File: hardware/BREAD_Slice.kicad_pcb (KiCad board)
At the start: 2 copper layers, 70 x 100 mm, 59 parts, among them J1 Conn_01x10_Socket, J2 Screw_Terminal_01x06, J3 Screw_Terminal_01x02, J4 Screw_Terminal_01x08, SW1 SW_DIP_x04, SW3 SW_SPDT, U1 AP63205, U10 CPC1002N, U11 CPC1002N, U12 NTGS4111PT1G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

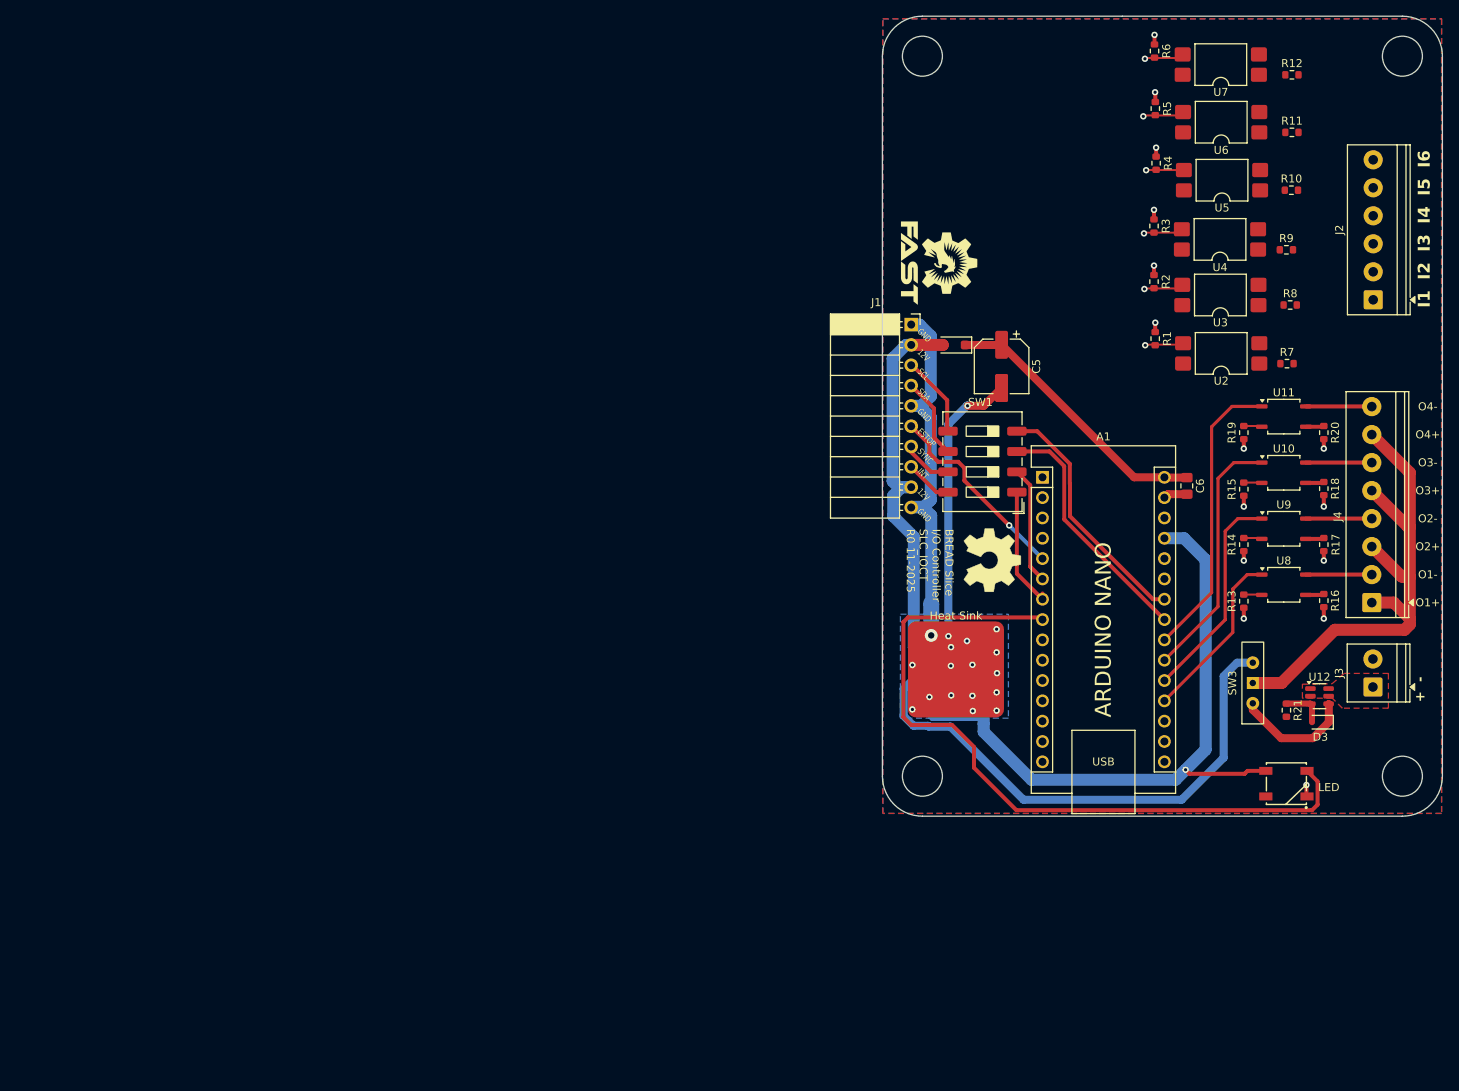
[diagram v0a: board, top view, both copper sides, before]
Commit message: revision of symbol attachment and clear out old layout and start new; kml-custom to kmlib-local
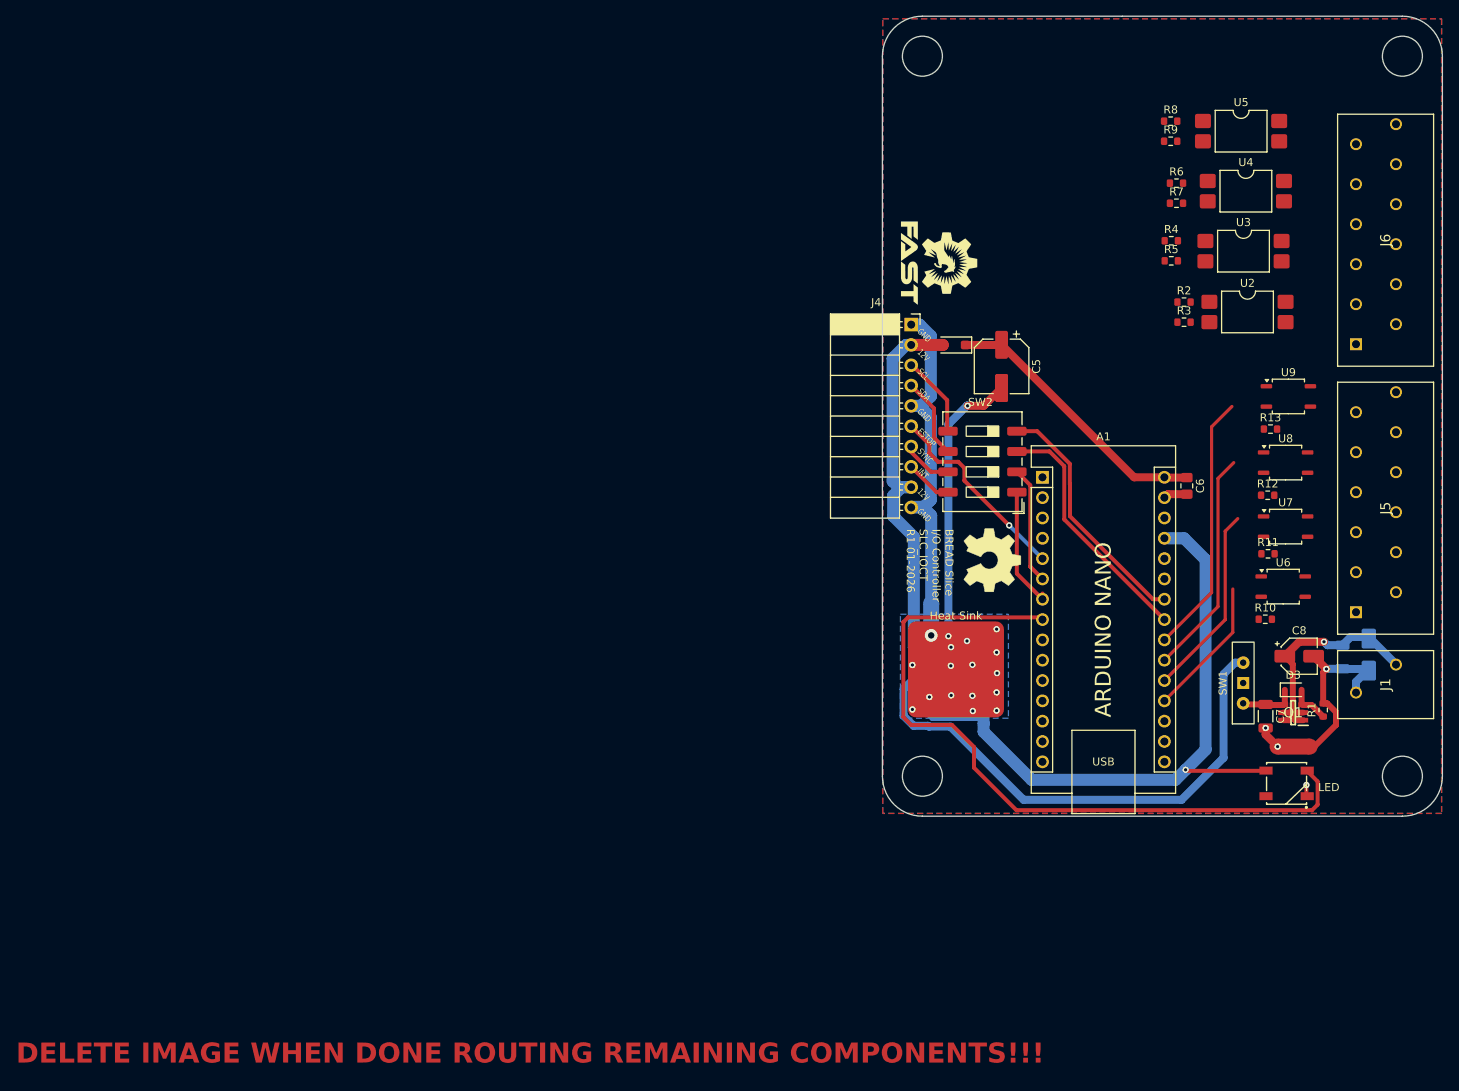
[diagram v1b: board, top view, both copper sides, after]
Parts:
- removed J2: Screw_Terminal_01x06, TerminalBlock_Phoenix:TerminalBlock_Phoenix_PT-1,5-6-3.5-H_1x06_P3.50mm_Horizontal
- removed J3: Screw_Terminal_01x02, TerminalBlock_Phoenix:TerminalBlock_Phoenix_PT-1,5-2-3.5-H_1x02_P3.50mm_Horizontal
- removed the J4 at (183.8, 113.1)
- removed R14, R15, R19: 2.4k, Resistor_SMD:R_0603_1608Metric
- removed R16, R17, R18, R20: 47, Resistor_SMD:R_0603_1608Metric
- removed R21: 100k, Resistor_SMD:R_0603_1608Metric
- removed U10, U11: CPC1002N, Package_SO:SOP-4_3.8x4.1mm_P2.54mm
- removed U12: NTGS4111PT1G, Package_TO_SOT_SMD:TSOT-23-6
- added C7: 100n, Capacitor_SMD:C_1206_3216Metric, F.Cu at (170.5, 127.3)
- added C8: 10u, Capacitor_SMD:CP_Elec_4x5.8, F.Cu at (174.7, 119.8)
- added C9: 100n, Capacitor_SMD:C_1206_3216Metric, B.Cu at (180.1, 119.9)
- added D4: SMAJ24CA, Diode_SMD:D_SMA, B.Cu at (183.4, 119.6)
- added J1: 1985195, KMLib_Connectors:1985195, F.Cu at (181.8, 127.6)
- added J5: 1990106, KMLib_Connectors:1990106, F.Cu at (181.8, 114.3)
- added J6: 1990106, KMLib_Connectors:1990106, F.Cu at (181.8, 80.8)
- added NT2: NetTie_2, NetTie:NetTie-2_SMD_Pad2.0mm, F.Cu at (174.0, 131.1)
- added Q1: NTGS4111PT1G, KMLib_IC_SMD:SOT95P275X110-6N, F.Cu at (173.9, 126.8)
- A1: footprint kml-custom:Arduino_Nano_Headers -> KMLib_Boards_Modules:Arduino_Nano_Headers
- D2: footprint kml-custom:WS2812-5050-4PIN -> KMLib_IC_SMD:WS2812-5050-4PIN
- HS1: footprint kml-custom:Thermal Pad -> KMLib_Mounting:Thermal Pad
- R1: value 1k -> 100k
- R10, R11, R12: value 1k -> 1.3k
- R13: value 2.4k -> 1.3k
- U1: footprint kml-custom:SOIC_05WU-7_DIO-M -> KMLib_IC_SMD:SOIC_05WU-7_DIO
- U6, U7: value LTV-817S -> CPC1002N; footprint Package_DIP:SMDIP-4_W9.53mm -> Package_SO:SOP-4_3.8x4.1mm_P2.54mm
- moved U6 58.6 mm to (172.7, 111.1), turned to 0 degrees
- moved U7 58.3 mm to (173.0, 103.6), turned to 0 degrees
- moved R10 53.7 mm to (170.5, 115.2)
- moved R11 52.8 mm to (170.8, 107.0)
- moved R12 52.6 mm to (170.8, 99.7)
- moved R1 50.9 mm to (177.7, 126.5)
- moved R8 27.4 mm to (158.6, 52.9)
- moved R7 24.3 mm to (159.4, 63.2)
- moved R13 21.8 mm to (171.1, 91.4), turned to 0 degrees
- moved R9 19.8 mm to (158.6, 55.4)
- moved R5 19.1 mm to (158.7, 70.4), turned to 0 degrees
- moved R6 16.7 mm to (159.4, 60.7), turned to 0 degrees
- moved U9 16.5 mm to (173.3, 87.3)
- moved U8 15.3 mm to (173.0, 95.6)
- moved R3 12.6 mm to (160.3, 78.0), turned to 0 degrees
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- renumbered J1 to J4, SW3 to SW1, SW1 to SW2
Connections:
- net Net-(D3-K) renamed /+24V
- A1 pad 10: /IN3 -> /OUT3
- A1 pad 11: /IN5 -> /OUT2
- A1 pad 12: /IN6 -> /OUT4
- A1 pad 13: /IN4 -> /slice_template/D10
- A1 pad 14: /IN2 -> /slice_template/D11/MOSI
- A1 pad 19: OUT1 -> /IN1
- A1 pad 20: OUT2 -> /IN2
- A1 pad 21: OUT3 -> /IN3
- A1 pad 22: OUT4 -> /IN4
- A1 pad 9: /IN1 -> /OUT1
- R1 pad 1: /IN1 -> Net-(D3-A)
- R1 pad 2: GND -> /Input Power Protection/INPUT_GND
- R10 pad 1: Net-(R10-Pad1) -> GND
- R10 pad 2: IN4B -> Net-(R10-Pad2)
- R11 pad 1: Net-(R11-Pad1) -> GND
- R11 pad 2: IN5B -> Net-(R11-Pad2)
- R12 pad 1: Net-(R12-Pad1) -> GND
- R12 pad 2: IN6B -> Net-(R12-Pad2)
- R13 pad 1: Net-(R13-Pad1) -> GND
- R13 pad 2: GND -> Net-(R13-Pad2)
- R2 pad 1: /IN2 -> /IN1
- R3 pad 1: /IN3 -> Net-(R3-Pad1)
- R3 pad 2: GND -> /IN1+
- R4 pad 1: /IN4 -> /IN2
- R5 pad 1: /IN5 -> Net-(R5-Pad1)
- R5 pad 2: GND -> /IN2+
- R6 pad 1: /IN6 -> /IN3
- R7 pad 2: Net-(J2-Pin_1) -> /IN3+
- R8 pad 1: Net-(R8-Pad1) -> /IN4
- R8 pad 2: Net-(J2-Pin_2) -> GND
- R9 pad 2: Net-(J2-Pin_3) -> /IN4+
- SW1 pad 1: VOUT -> /VFIELD
- U2 pad 1: Net-(R7-Pad1) -> Net-(R3-Pad1)
- U2 pad 2: GND -> /IN1-
- U3 pad 1: Net-(R8-Pad1) -> Net-(R5-Pad1)
- U3 pad 2: GND -> /IN2-
- U4 pad 1: Net-(R9-Pad1) -> Net-(R7-Pad1)
- U4 pad 2: GND -> /IN3-
- U5 pad 1: Net-(R10-Pad1) -> Net-(R9-Pad1)
- U5 pad 2: GND -> /IN4-
- U6 pad 1: Net-(R11-Pad1) -> /OUT1
- U6 pad 2: GND -> Net-(R10-Pad2)
- U6 pad 3: /IN5 -> /OUT1-
- U6 pad 4: +5V -> /OUT1+
- U7 pad 1: Net-(R12-Pad1) -> /OUT2
- U7 pad 2: GND -> Net-(R11-Pad2)
- U7 pad 3: /IN6 -> /OUT2-
- U7 pad 4: +5V -> /OUT2+
- U8 pad 1: OUT1 -> /OUT3
- U8 pad 2: Net-(R13-Pad1) -> Net-(R12-Pad2)
- U8 pad 3: Net-(R16-Pad1) -> /OUT3-
- U8 pad 4: OUT1B -> /OUT3+
- U9 pad 1: OUT2 -> /OUT4
- U9 pad 2: Net-(R14-Pad1) -> Net-(R13-Pad2)
- U9 pad 3: Net-(R17-Pad1) -> /OUT4-
- U9 pad 4: OUT2B -> /OUT4+
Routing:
- net VOUT: track 66.9 -> 0.00 mm
- net OUT4: track 36.4 -> 0.00 mm
- net /Input Power Protection/INPUT_VDD: track 0.00 -> 32.1 mm, vias 0 -> 1
- net OUT3: track 31.8 -> 0.00 mm
- net /IN4: track 4.73 -> 32.7 mm, vias 1 -> 0
- net OUT2: track 27.0 -> 0.00 mm
- net /Input Power Protection/INPUT_GND: track 0.00 -> 23.7 mm, vias 0 -> 1
- net /IN3: track 4.95 -> 28.3 mm, vias 1 -> 0
- net OUT1: track 21.9 -> 0.00 mm
- net /IN2: track 4.95 -> 24.0 mm, vias 1 -> 0
- net GND: track 73.4 -> 59.0 mm, vias 33 -> 21
- net /IN1: track 4.84 -> 17.5 mm, vias 1 -> 0
- net OUT4B: track 8.26 -> 0.00 mm
- net OUT3B: track 8.25 -> 0.00 mm
- net OUT2B: track 8.25 -> 0.00 mm
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- removed copper zone on F.Cu, net /24V
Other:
- board text added: "BREAD Slice I/O Controller SLC_IOCT R1 01-2026"
- board text added: "DELETE IMAGE WHEN DONE ROUTING REMAINING COMPONENTS!!!"
- board text removed: "+ -"
- board text removed: "BREAD Slice I/O Controller SLC_IOCT R0 11-2025"
- board text removed: "I1"
- board text removed: "I2"
- board text removed: "I3"
- board text removed: "I4"
- board text removed: "I5"
- board text removed: "I6"
- board text removed: "O1+"
- board text removed: "O1-"
- board text removed: "O2+"
- board text removed: "O2-"
- board text removed: "O3+"
- board text removed: "O3-"
- board text removed: "O4+"
- board text removed: "O4-"

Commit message: rerouted using PTSA connectors
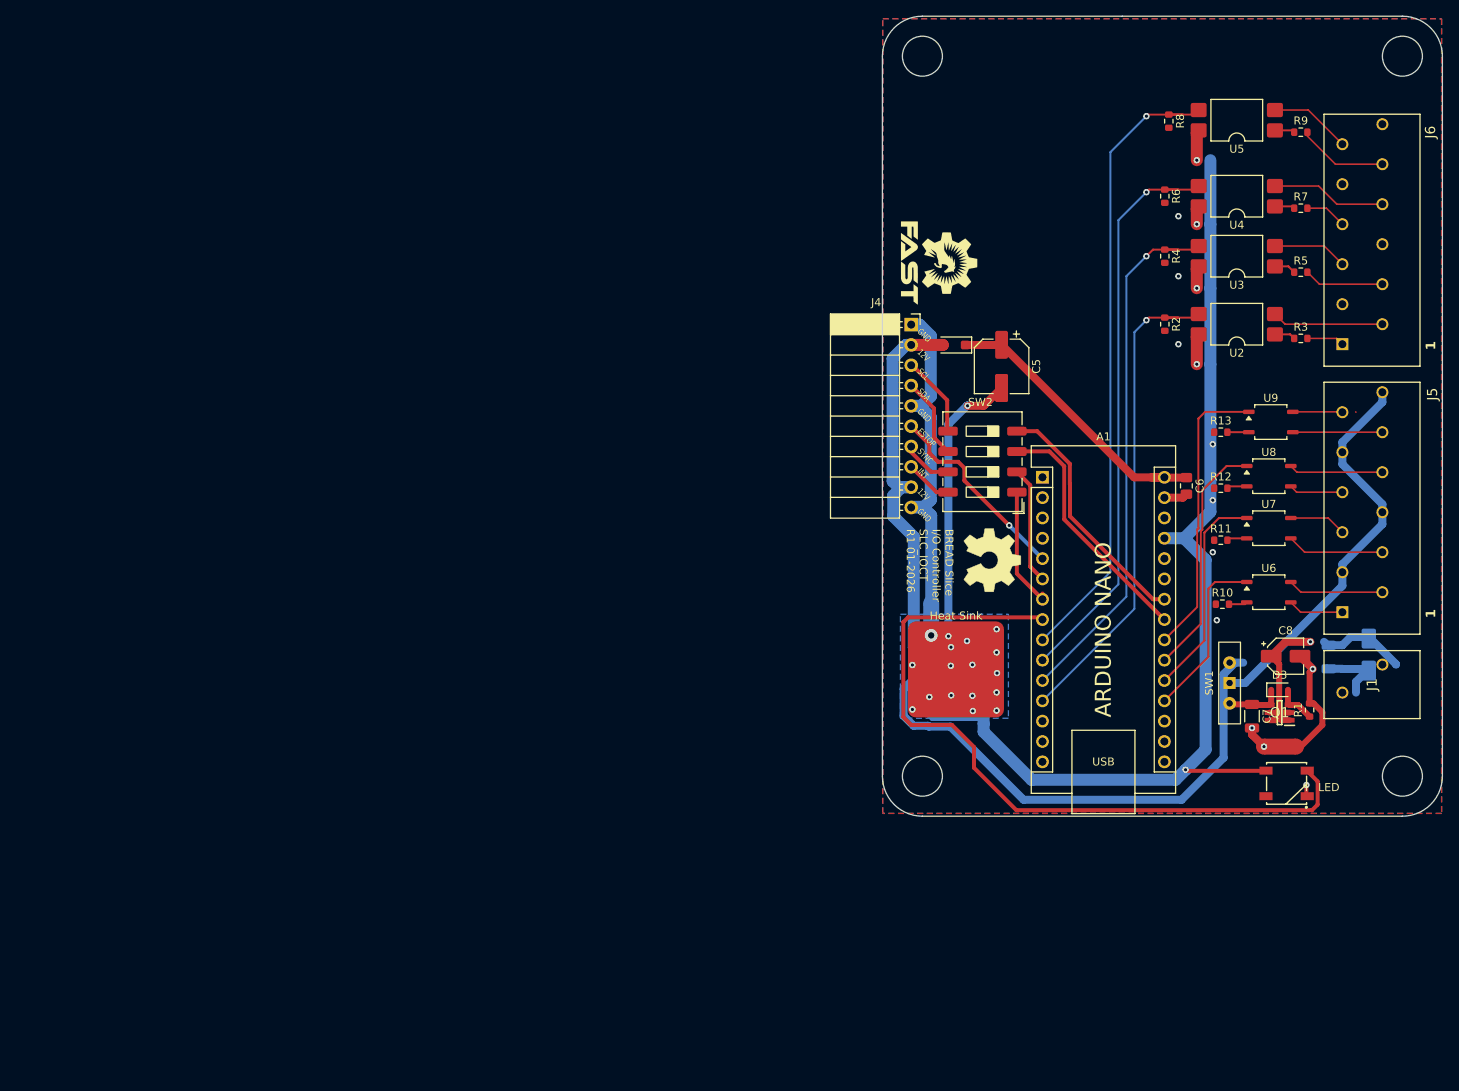
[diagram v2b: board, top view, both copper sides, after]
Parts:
- moved R9 16.3 mm to (174.9, 54.3)
- moved R5 16.3 mm to (174.9, 71.8)
- moved R7 15.6 mm to (174.9, 63.8)
- moved R3 14.7 mm to (174.9, 80.1)
- moved R13 6.22 mm to (164.9, 91.8)
- moved R11 6.14 mm to (164.9, 105.3)
- moved R12 5.93 mm to (164.9, 98.8)
- moved R10 5.68 mm to (165.1, 113.3)
- moved U9 3.88 mm to (171.2, 90.5)
- moved R2 3.66 mm to (157.9, 78.3), turned to -90 degrees
- moved U8 2.70 mm to (170.9, 97.3)
- moved R6 2.19 mm to (157.9, 62.3), turned to -90 degrees
- moved U7 2.11 mm to (170.9, 103.8)
- moved R4 2.09 mm to (157.9, 69.8), turned to -90 degrees
- moved U2 2.03 mm to (166.9, 78.3), turned to 180 degrees
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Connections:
- A1 pad 10: /OUT3 -> /IN3
- A1 pad 11: /OUT2 -> /IN2
- A1 pad 12: /OUT4 -> /IN1
- A1 pad 19: /IN1 -> /OUT1
- A1 pad 20: /IN2 -> /OUT2
- A1 pad 21: /IN3 -> /OUT3
- A1 pad 22: /IN4 -> /OUT4
- A1 pad 9: /OUT1 -> /IN4
- J5 pad 1: /OUT1+ -> /OUT1-
- J5 pad 2: /OUT1- -> /OUT1+
- U7 pad 3: /OUT2- -> /OUT2+
- U7 pad 4: /OUT2+ -> /OUT2-
- U8 pad 3: /OUT3- -> /OUT3+
- U8 pad 4: /OUT3+ -> /OUT3-
- U9 pad 3: /OUT4- -> /OUT4+
- U9 pad 4: /OUT4+ -> /OUT4-
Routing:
- net +5V: track 96.2 -> 157.7 mm, vias 1 -> 5
- net /VFIELD: track 0.00 -> 49.1 mm
- net /IN4: track 32.7 -> 79.4 mm, vias 0 -> 1
- net /IN3: track 28.3 -> 72.4 mm, vias 0 -> 1
- net /IN1: track 17.5 -> 61.5 mm, vias 0 -> 1
- net /IN2: track 24.0 -> 67.2 mm, vias 0 -> 1
- net /OUT4: track 0.00 -> 36.1 mm
- net /OUT3: track 0.00 -> 30.0 mm
- net /OUT2: track 0.00 -> 26.6 mm
- net /OUT1: track 0.00 -> 21.4 mm
- net /IN3-: track 0.00 -> 14.4 mm
- net /IN1-: track 0.00 -> 14.0 mm
- net /OUT2+: track 0.00 -> 12.2 mm
- net /OUT1+: track 0.00 -> 12.0 mm
- net /OUT3-: track 0.00 -> 11.8 mm
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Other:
- board text added: "1"
- board text removed: "DELETE IMAGE WHEN DONE ROUTING REMAINING COMPONENTS!!!"
